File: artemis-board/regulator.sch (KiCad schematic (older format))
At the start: 30 parts, among them Q5 AO3401A, Q6 AO3401A, Q7 2N7002, Q8 2N7002, Q9 AO3401A, U10 FP6291LR, U11 ME6210A33P, U12 ME6210A33P

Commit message: increased output caps of voltage regulators
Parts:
- added C15, C19, C20: 22µF, Capacitor_SMD:C_0805_2012Metric, symbol Device:C
- C16, C17, C18: value 10µF -> 22µF; footprint Capacitor_SMD:C_0603_1608Metric_Pad1.05x0.95mm_HandSolder -> Capacitor_SMD:C_0805_2012Metric; LCSC C19702 -> C45783
- C23: value 0.1µF -> 1µF; LCSC C14858 -> C15849
- renumbered C15 to C6, C14 to C7
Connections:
- net 3v3: now also C19.1
- net 3v3_MCU: now also C20.1
- net 5V: now also C15.1
- net GND: now also C15.2, C19.2, C20.2
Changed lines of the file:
@@
 $EndComp
 $Comp
-L Device:C C14
+L Device:C C7
 U 1 1 5F85115B
 P 7600 3400
-F 0 "C14" H 7715 3446 50  0000 L CNN
+F 0 "C7" H 7715 3446 50  0000 L CNN
 F 1 "0.1µF" H 7715 3355 50  0000 L CNN
 F 2 "Capacitor_SMD:C_0603_1608Metric_Pad1.05x0.95mm_HandSolder" H 7638 3250 50  0001 C CNN
@@
 $EndComp
 $Comp
-L Device:C C15
+L Device:C C6
 U 1 1 5F85228B
 P 2900 3200
-F 0 "C15" H 3015 3246 50  0000 L CNN
+F 0 "C6" H 3015 3246 50  0000 L CNN
 F 1 "0.1µF" H 3015 3155 50  0000 L CNN
 F 2 "Capacitor_SMD:C_0603_1608Metric_Pad1.05x0.95mm_HandSolder" H 2938 3050 50  0001 C CNN
@@
 P 8950 3300
 F 0 "C16" H 9065 3346 50  0000 L CNN
-F 1 "10µF" H 9065 3255 50  0000 L CNN
-F 2 "Capacitor_SMD:C_0603_1608Metric_Pad1.05x0.95mm_HandSolder" H 8988 3150 50  0001 C CNN
+F 1 "22µF" H 9065 3255 50  0000 L CNN
+F 2 "Capacitor_SMD:C_0805_2012Metric" H 8988 3150 50  0001 C CNN
 F 3 "~" H 8950 3300 50  0001 C CNN
-F 4 "C19702" H 8950 3300 50  0001 C CNN "LCSC"
+F 4 "C45783" H 8950 3300 50  0001 C CNN "LCSC"
 	1    8950 3300
 	1    0    0    -1
@@
 P 4650 3200
 F 0 "C18" H 4765 3246 50  0000 L CNN
-F 1 "10µF" H 4765 3155 50  0000 L CNN
-F 2 "Capacitor_SMD:C_0603_1608Metric_Pad1.05x0.95mm_HandSolder" H 4688 3050 50  0001 C CNN
+F 1 "22µF" H 4765 3155 50  0000 L CNN
+F 2 "Capacitor_SMD:C_0805_2012Metric" H 4688 3050 50  0001 C CNN
 F 3 "~" H 4650 3200 50  0001 C CNN
-F 4 "C19702" H 4650 3200 50  0001 C CNN "LCSC"
+F 4 "C45783" H 4650 3200 50  0001 C CNN "LCSC"
 	1    4650 3200
 	1    0    0    -1
@@
 3.3V Sensor Regulator\n
 Wire Notes Line
-	6200 4300 6200 6150
+	8200 4300 8200 6150
 Wire Notes Line
 	1200 6150 1200 4300
@@
 Text Label 1750 3000 0    50   ~ 0
 VBAT
-Text Label 5100 3000 2    50   ~ 0
-3v3_MCU
-Text Label 9250 3050 2    50   ~ 0
+Text Label 9650 3050 2    50   ~ 0
 3v3
 Text Label 5950 3550 0    50   ~ 0
@@
 Text Label 1750 3400 0    50   ~ 0
 INT
-Text Label 6000 4900 2    50   ~ 0
+Text Label 6850 4900 2    50   ~ 0
 5V
 Text Label 5900 3050 0    50   ~ 0
 VBAT
 Wire Wire Line
-	8950 3050 9250 3050
+	8950 3050 9400 3050
 Wire Wire Line
 	5950 3550 6400 3550
@@
 Connection ~ 4650 3000
 Wire Wire Line
-	4650 3000 5100 3000
-Wire Wire Line
 	4150 3050 4150 3000
 Connection ~ 4150 3000
@@
 P 2700 3400
 F 0 "C23" V 2850 3450 50  0000 L CNN
-F 1 "0.1µF" V 2850 3200 50  0000 L CNN
+F 1 "1µF" V 2850 3200 50  0000 L CNN
 F 2 "Capacitor_SMD:C_0603_1608Metric_Pad1.05x0.95mm_HandSolder" H 2738 3250 50  0001 C CNN
 F 3 "~" H 2700 3400 50  0001 C CNN
-F 4 "C14858" H 2700 3400 50  0001 C CNN "LCSC"
+F 4 "C15849" H 2700 3400 50  0001 C CNN "LCSC"
 	1    2700 3400
 	0    1    1    0
@@
 Wire Wire Line
 	7250 3750 6700 3750
-Wire Notes Line
-	1200 4300 6200 4300
-Wire Notes Line
-	1200 6150 6200 6150
 Wire Wire Line
 	2550 5600 2950 5600
@@
 	4250 4900 4250 5100
 Wire Wire Line
-	5800 4900 6000 4900
+	5800 4900 6250 4900
 $Comp
 L FP6291LR:FP6291LR U10
@@
 Wire Wire Line
 	4200 5100 4250 5100
-$Comp
-L Device:C C17
-U 1 1 5F86990F
-P 5800 5200
-F 0 "C17" H 5915 5246 50  0000 L CNN
-F 1 "10µF" H 5915 5155 50  0000 L CNN
-F 2 "Capacitor_SMD:C_0603_1608Metric_Pad1.05x0.95mm_HandSolder" H 5838 5050 50  0001 C CNN
-F 3 "~" H 5800 5200 50  0001 C CNN
-F 4 "C19702" H 5800 5200 50  0001 C CNN "LCSC"
-	1    5800 5200
-	1    0    0    -1
-$EndComp
 Connection ~ 5800 4900
 Wire Wire Line
 	5800 4900 5800 5050
-Wire Wire Line
-	5800 5350 5800 5600
 Wire Wire Line
 	5800 5600 5250 5600
@@
 Wire Notes Line
 	600  600  600  2050
+$Comp
+L Device:C C19
+U 1 1 60374573
+P 9400 3300
+F 0 "C19" H 9515 3346 50  0000 L CNN
+F 1 "22µF" H 9515 3255 50  0000 L CNN
+F 2 "Capacitor_SMD:C_0805_2012Metric" H 9438 3150 50  0001 C CNN
+F 3 "~" H 9400 3300 50  0001 C CNN
+F 4 "C45783" H 9400 3300 50  0001 C CNN "LCSC"
+	1    9400 3300
+	1    0    0    -1
+$EndComp
+Wire Wire Line
+	9400 3450 9400 3750
+$Comp
+L Device:C C20
+U 1 1 6037883A
+P 5100 3200
+F 0 "C20" H 5215 3246 50  0000 L CNN
+F 1 "22µF" H 5215 3155 50  0000 L CNN
+F 2 "Capacitor_SMD:C_0805_2012Metric" H 5138 3050 50  0001 C CNN
+F 3 "~" H 5100 3200 50  0001 C CNN
+F 4 "C45783" H 5100 3200 50  0001 C CNN "LCSC"
+	1    5100 3200
+	1    0    0    -1
+$EndComp
+Wire Wire Line
+	5100 3350 5100 3400
+Wire Wire Line
+	5100 3400 4650 3400
+Connection ~ 4650 3400
+Wire Wire Line
+	5100 3050 5100 3000
+Wire Wire Line
+	4650 3000 5100 3000
+Text Label 5350 3000 2    50   ~ 0
+3v3_MCU
+Wire Wire Line
+	5350 3000 5100 3000
+Connection ~ 5100 3000
+Wire Wire Line
+	8950 3750 9400 3750
+Connection ~ 8950 3750
+Wire Wire Line
+	9400 3150 9400 3050
+Connection ~ 9400 3050
+Wire Wire Line
+	9400 3050 9650 3050
+Wire Notes Line
+	1200 4300 8200 4300
+Wire Notes Line
+	1200 6150 8200 6150
+Wire Wire Line
+	5800 5350 5800 5600
+$Comp
+L Device:C C17
+U 1 1 5F86990F
+P 5800 5200
+F 0 "C17" H 5915 5246 50  0000 L CNN
+F 1 "22µF" H 5915 5155 50  0000 L CNN
+F 2 "Capacitor_SMD:C_0805_2012Metric" H 5838 5050 50  0001 C CNN
+F 3 "~" H 5800 5200 50  0001 C CNN
+F 4 "C45783" H 5800 5200 50  0001 C CNN "LCSC"
+	1    5800 5200
+	1    0    0    -1
+$EndComp
+Wire Wire Line
+	6250 5350 6250 5600
+$Comp
+L Device:C C15
+U 1 1 603B8C1B
+P 6250 5200
+F 0 "C15" H 6365 5246 50  0000 L CNN
+F 1 "22µF" H 6365 5155 50  0000 L CNN
+F 2 "Capacitor_SMD:C_0805_2012Metric" H 6288 5050 50  0001 C CNN
+F 3 "~" H 6250 5200 50  0001 C CNN
+F 4 "C45783" H 6250 5200 50  0001 C CNN "LCSC"
+	1    6250 5200
+	1    0    0    -1
+$EndComp
+Wire Wire Line
+	6250 5600 5800 5600
+Connection ~ 5800 5600
+Wire Wire Line
+	6250 5050 6250 4900
+Connection ~ 6250 4900
+Wire Wire Line
+	6250 4900 6850 4900
 $EndSCHEMATC

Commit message: swapped R15 for 24k
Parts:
- R15: value 22k -> 24k; LCSC C31850 -> C23352
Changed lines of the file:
@@
 P 4750 5450
 F 0 "R15" H 4820 5496 50  0000 L CNN
-F 1 "22k" H 4820 5405 50  0000 L CNN
+F 1 "24k" H 4820 5405 50  0000 L CNN
 F 2 "Resistor_SMD:R_0603_1608Metric_Pad1.05x0.95mm_HandSolder" V 4680 5450 50  0001 C CNN
 F 3 "~" H 4750 5450 50  0001 C CNN
-F 4 "C31850" H 4750 5450 50  0001 C CNN "LCSC"
+F 4 "C23352" H 4750 5450 50  0001 C CNN "LCSC"
 	1    4750 5450
 	1    0    0    -1

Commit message: added cirquit to measure Vbat with esp in case of fuel gauge shortage
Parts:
- R17: value 22k -> 24k; LCSC C31850 -> C23352
- renumbered R19 to R15, R15 to R18

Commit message: added comment with alternative 3v3 regulators
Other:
- note added: "Alternative 3v3 regulators: C50936, C111686, C236673"
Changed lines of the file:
@@
 	1    0    0    -1
 $EndComp
+Text Notes 4600 2100 0    50   ~ 0
+Alternative 3v3 regulators: C50936, C111686, C236673
 $EndSCHEMATC

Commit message: changed the layout a bit and removed TP on boost converter
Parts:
- removed TP5: TestPoint, TestPoint:TestPoint_Pad_1.5x1.5mm, symbol Connector:TestPoint
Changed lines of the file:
@@
 Wire Wire Line
 	4150 5600 4150 5700
-Wire Wire Line
-	4100 4900 4250 4900
-Connection ~ 4100 4900
 Connection ~ 4250 4900
 Wire Wire Line
@@
 	1    0    0    -1
 $EndComp
-Wire Wire Line
-	4000 4900 4100 4900
 Wire Wire Line
 	3300 5250 3300 5100
@@
 	1    3850 5250
 	-1   0    0    -1
-$EndComp
-$Comp
-L Connector:TestPoint TP5
-U 1 1 5F9A2164
-P 4100 4900
-F 0 "TP5" H 4050 5100 50  0000 L CNN
-F 1 "TestPoint" H 4158 4927 50  0001 L CNN
-F 2 "TestPoint:TestPoint_Pad_1.5x1.5mm" H 4300 4900 50  0001 C CNN
-F 3 "~" H 4300 4900 50  0001 C CNN
-	1    4100 4900
-	1    0    0    -1
 $EndComp
 $Comp
@@
 Text Notes 4600 2100 0    50   ~ 0
 Alternative 3v3 regulators: C50936, C111686, C236673
+Wire Wire Line
+	4000 4900 4250 4900
 $EndSCHEMATC

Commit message: increased value of R17 to decrease 5v overcurrent protection
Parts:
- R17: value 24k -> 39k; LCSC C23352 -> C23153
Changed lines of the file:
@@
 P 3300 5400
 F 0 "R17" H 3370 5446 50  0000 L CNN
-F 1 "24k" H 3370 5355 50  0000 L CNN
+F 1 "39k" H 3370 5355 50  0000 L CNN
 F 2 "Resistor_SMD:R_0603_1608Metric_Pad1.05x0.95mm_HandSolder" V 3230 5400 50  0001 C CNN
 F 3 "~" H 3300 5400 50  0001 C CNN
-F 4 "C23352" H 3300 5400 50  0001 C CNN "LCSC"
+F 4 "C23153" H 3300 5400 50  0001 C CNN "LCSC"
 	1    3300 5400
 	1    0    0    -1

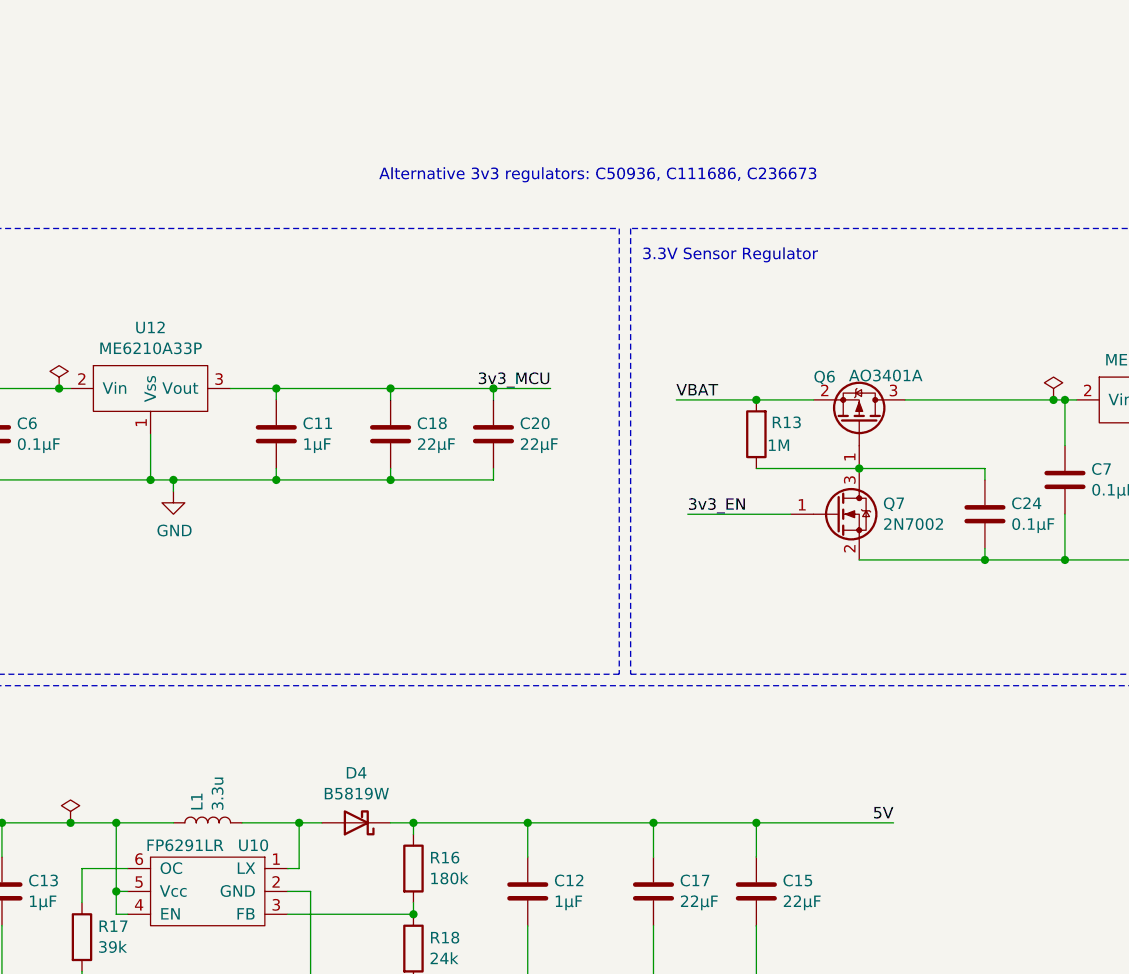
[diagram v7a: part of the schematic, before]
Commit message: corrected inductor value text field
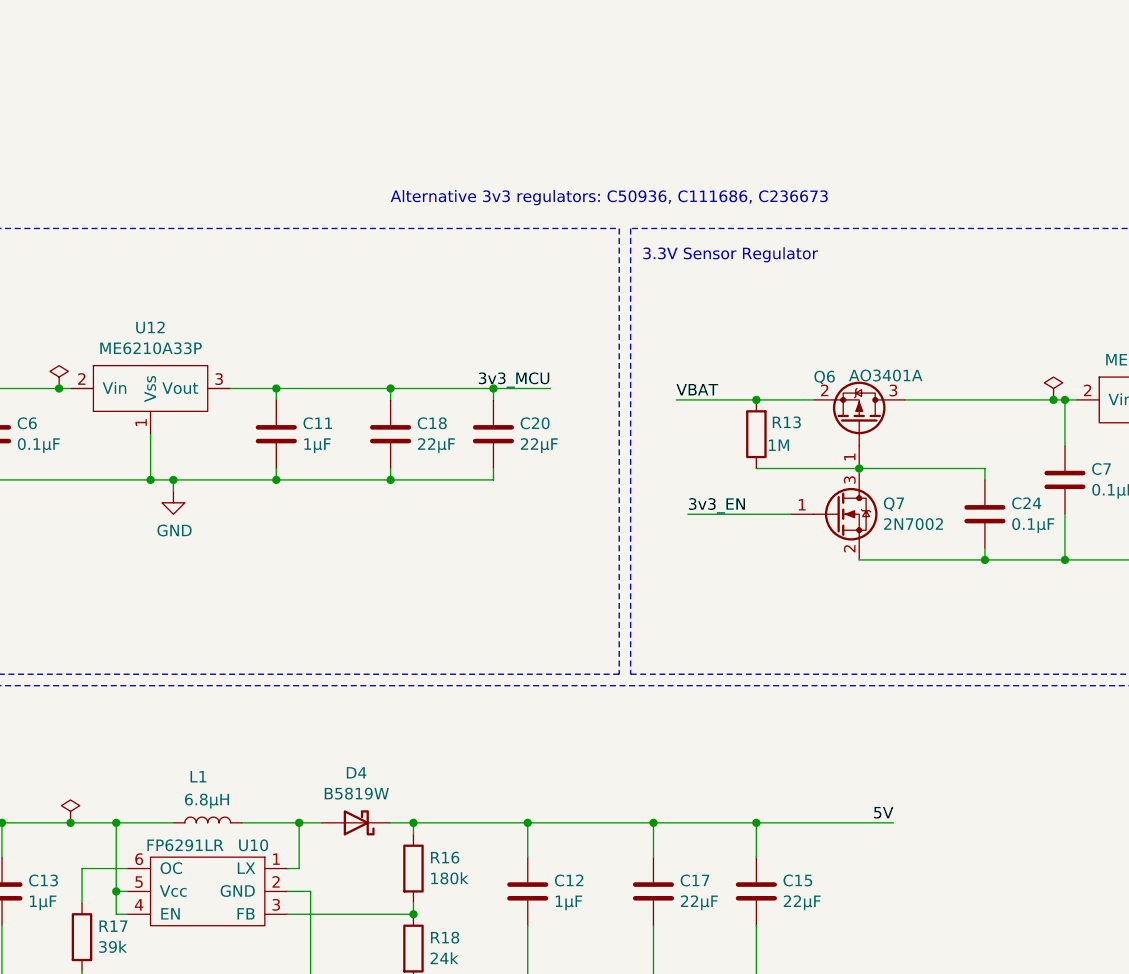
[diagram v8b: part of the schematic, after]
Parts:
- L1: value 3.3u -> 6.8µH
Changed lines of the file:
@@
 U 1 1 5F829D65
 P 3850 4900
-F 0 "L1" H 3902 4946 50  0000 L CNN
-F 1 "3.3u" H 3902 4855 50  0000 L CNN
+F 0 "L1" V 4050 4900 50  0000 L CNN
+F 1 "6.8µH" V 3950 4800 50  0000 L CNN
 F 2 "Inductor_SMD:L_Bourns_SRP7028A_7.3x6.6mm" H 3850 4900 50  0001 C CNN
 F 3 "https://datasheet.lcsc.com/szlcsc/1811091611_Sunltech-Tech-SLO0630H6R8MTT_C207841.pdf" H 3850 4900 50  0001 C CNN
@@
 	1    0    0    -1
 $EndComp
-Text Notes 4600 2100 0    50   ~ 0
+Text Notes 4650 2200 0    50   ~ 0
 Alternative 3v3 regulators: C50936, C111686, C236673
 Wire Wire Line
